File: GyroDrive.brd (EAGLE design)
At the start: 15.4 x 13.7 mm, 41 parts, among them IC1 AD8235, IC2 AD8235, IC3 AD8235, IC4 AD8235

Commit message: Removed copper from underneath MPU-9250
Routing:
- net DGND: track 19.3 -> 16.8 mm
- net VDD: track 16.7 -> 15.4 mm, vias 5 -> 6
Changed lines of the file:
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@@
 <wire x1="5.715" y1="3.81" x2="5.715" y2="4.826" width="0.1524" layer="16"/>
 <via x="5.715" y="4.826" extent="1-16" drill="0.254"/>
-<wire x1="5.715" y1="4.826" x2="5.715" y2="4.572" width="0" layer="19" extent="1-16"/>
 <wire x1="10.791" y1="3.81" x2="10.791" y2="4.826" width="0.1524" layer="16"/>
 <wire x1="10.791" y1="4.826" x2="10.795" y2="4.826" width="0.1524" layer="16"/>
 <via x="10.795" y="4.826" extent="1-16" drill="0.254"/>
-<wire x1="10.795" y1="4.826" x2="10.795" y2="4.699" width="0" layer="19" extent="1-16"/>
 <wire x1="10.791" y1="3.81" x2="10.791" y2="3.294" width="0.1524" layer="16"/>
 <wire x1="10.791" y1="3.294" x2="10.783" y2="3.294" width="0.1524" layer="16"/>
@@
 <wire x1="8.251" y1="4.826" x2="8.255" y2="4.826" width="0.1524" layer="16"/>
 <via x="8.255" y="4.826" extent="1-16" drill="0.254"/>
-<wire x1="8.255" y1="4.826" x2="8.255" y2="4.699" width="0" layer="19" extent="1-16"/>
 <wire x1="13.3056" y1="3.8608" x2="13.3056" y2="4.826" width="0.1524" layer="16"/>
 <wire x1="13.3056" y1="4.826" x2="13.335" y2="4.826" width="0.1524" layer="16"/>
 <via x="13.335" y="4.826" extent="1-16" drill="0.254"/>
-<wire x1="13.335" y1="4.826" x2="13.335" y2="4.699" width="0" layer="19" extent="1-16"/>
 <wire x1="13.3056" y1="3.8608" x2="13.3056" y2="3.294" width="0.1524" layer="16"/>
 <wire x1="13.3056" y1="3.294" x2="13.323" y2="3.294" width="0.1524" layer="16"/>
@@
 <wire x1="8.767" y1="4.445" x2="8.763" y2="4.445" width="0.1524" layer="16"/>
 <via x="8.763" y="4.445" extent="1-16" drill="0.254"/>
-<wire x1="8.763" y1="4.445" x2="8.763" y2="4.318" width="0" layer="19" extent="1-16"/>
 <wire x1="11.823" y1="2.794" x2="11.303" y2="2.794" width="0.1524" layer="16"/>
 <wire x1="11.303" y1="2.794" x2="11.303" y2="3.294" width="0.1524" layer="16"/>
@@
 <wire x1="11.303" y1="3.81" x2="11.303" y2="4.445" width="0.1524" layer="16"/>
 <via x="11.303" y="4.445" extent="1-16" drill="0.254"/>
-<wire x1="11.303" y1="4.445" x2="11.303" y2="4.318" width="0" layer="19" extent="1-16"/>
 <wire x1="11.307" y1="3.81" x2="11.307" y2="3.294" width="0.1524" layer="16"/>
 <wire x1="11.307" y1="3.294" x2="11.303" y2="3.294" width="0.1524" layer="16"/>
@@
 <wire x1="6.223" y1="3.814" x2="6.223" y2="4.445" width="0.1524" layer="16"/>
 <via x="6.223" y="4.445" extent="1-16" drill="0.254"/>
-<wire x1="6.223" y1="4.445" x2="6.223" y2="4.318" width="0" layer="19" extent="1-16"/>
 <wire x1="6.223" y1="3.302" x2="6.227" y2="3.306" width="0.1524" layer="16"/>
 <wire x1="6.227" y1="3.306" x2="6.227" y2="3.81" width="0.1524" layer="16"/>
@@
 <wire x1="3.683" y1="3.814" x2="3.683" y2="4.826" width="0.1524" layer="16"/>
 <via x="3.683" y="4.826" extent="1-16" drill="0.254"/>
-<wire x1="3.683" y1="4.826" x2="3.683" y2="4.699" width="0" layer="19" extent="1-16"/>
 <wire x1="3.683" y1="3.302" x2="3.687" y2="3.306" width="0.1524" layer="16"/>
 <wire x1="3.687" y1="3.306" x2="3.687" y2="3.81" width="0.1524" layer="16"/>
@@
 <wire x1="7.747" y1="3.81" x2="7.747" y2="4.445" width="0.1524" layer="16"/>
 <via x="7.747" y="4.445" extent="1-16" drill="0.254"/>
-<wire x1="7.747" y1="4.445" x2="7.747" y2="4.191" width="0" layer="19" extent="1-16"/>
 <wire x1="10.291" y1="3.81" x2="10.291" y2="4.445" width="0.1524" layer="16"/>
 <wire x1="10.291" y1="4.445" x2="10.287" y2="4.445" width="0.1524" layer="16"/>
 <via x="10.287" y="4.445" extent="1-16" drill="0.254"/>
-<wire x1="10.287" y1="4.445" x2="10.287" y2="4.318" width="0" layer="19" extent="1-16"/>
 <wire x1="10.291" y1="3.81" x2="10.291" y2="3.294" width="0.1524" layer="16"/>
 <wire x1="10.291" y1="3.294" x2="10.283" y2="3.294" width="0.1524" layer="16"/>
@@
 <wire x1="9.267" y1="4.826" x2="9.271" y2="4.826" width="0.1524" layer="16"/>
 <via x="9.271" y="4.826" extent="1-16" drill="0.254"/>
-<wire x1="9.271" y1="4.826" x2="9.271" y2="4.699" width="0" layer="19" extent="1-16"/>
 <wire x1="11.807" y1="3.81" x2="11.807" y2="4.826" width="0.1524" layer="16"/>
 <wire x1="11.807" y1="4.826" x2="11.811" y2="4.826" width="0.1524" layer="16"/>
 <via x="11.811" y="4.826" extent="1-16" drill="0.254"/>
-<wire x1="11.811" y1="4.826" x2="11.811" y2="4.699" width="0" layer="19" extent="1-16"/>
 <wire x1="12.8056" y1="3.8608" x2="12.8056" y2="4.445" width="0.1524" layer="16"/>
 <wire x1="12.8056" y1="4.445" x2="12.827" y2="4.445" width="0.1524" layer="16"/>
 <via x="12.827" y="4.445" extent="1-16" drill="0.254"/>
-<wire x1="12.827" y1="4.445" x2="12.827" y2="4.318" width="0" layer="19" extent="1-16"/>
 <wire x1="12.8056" y1="3.8608" x2="12.8056" y2="3.294" width="0.1524" layer="16"/>
 <wire x1="12.8056" y1="3.294" x2="12.823" y2="3.294" width="0.1524" layer="16"/>
@@
 <wire x1="6.731" y1="3.814" x2="6.731" y2="4.826" width="0.1524" layer="16"/>
 <via x="6.731" y="4.826" extent="1-16" drill="0.254"/>
-<wire x1="6.731" y1="4.826" x2="6.731" y2="4.699" width="0" layer="19" extent="1-16"/>
 <wire x1="5.211" y1="3.81" x2="5.207" y2="3.814" width="0.1524" layer="16"/>
 <wire x1="5.207" y1="3.814" x2="5.207" y2="4.445" width="0.1524" layer="16"/>
 <via x="5.207" y="4.445" extent="1-16" drill="0.254"/>
-<wire x1="5.207" y1="4.445" x2="5.207" y2="4.191" width="0" layer="19" extent="1-16"/>
 <wire x1="5.211" y1="3.81" x2="5.203" y2="3.802" width="0.1524" layer="16"/>
 <wire x1="5.203" y1="3.802" x2="5.203" y2="3.294" width="0.1524" layer="16"/>
@@
 <wire x1="4.191" y1="3.814" x2="4.191" y2="4.445" width="0.1524" layer="16"/>
 <via x="4.191" y="4.445" extent="1-16" drill="0.254"/>
-<wire x1="4.191" y1="4.445" x2="4.191" y2="4.318" width="0" layer="19" extent="1-16"/>
 </signal>
 <signal name="S1">
@@
 <wire x1="11.034" y1="11.6078" x2="10.684" y2="11.557" width="0.1524" layer="1"/>
 <wire x1="10.684" y1="11.557" x2="10.684" y2="10.6932" width="0.1524" layer="1"/>
-<wire x1="10.684" y1="9.6932" x2="10.684" y2="10.6932" width="0.1524" layer="1"/>
 <contactref element="U$3" pad="2"/>
 <contactref element="C13" pad="2"/>
@@
 <wire x1="10.834" y1="12.7" x2="9.906" y2="12.7" width="0.254" layer="1"/>
 <via x="9.906" y="12.7" extent="1-16" drill="0.254"/>
-<wire x1="10.084" y1="9.6932" x2="10.684" y2="9.6932" width="0.1524" layer="1"/>
-<wire x1="10.684" y1="9.6932" x2="10.6934" y2="9.6932" width="0.1524" layer="1"/>
-<wire x1="10.6934" y1="9.6932" x2="10.668" y2="11.557" width="0.1524" layer="1"/>
 <wire x1="10.668" y1="11.557" x2="10.834" y2="11.557" width="0.1524" layer="1"/>
 <wire x1="10.834" y1="11.557" x2="10.834" y2="12.7" width="0.254" layer="1"/>
@@
 <via x="5.207" y="6.731" extent="1-16" drill="0.254"/>
 <wire x1="5.207" y1="6.731" x2="5.207" y2="7.366" width="0.254" layer="15"/>
+<wire x1="10.084" y1="9.6932" x2="9.144" y2="9.6932" width="0.1524" layer="1"/>
+<wire x1="9.144" y1="9.6932" x2="9.144" y2="9.652" width="0.1524" layer="1"/>
 </signal>
 <signal name="SDA">
@@
 <wire x1="13.284" y1="8.8932" x2="14.4526" y2="8.8932" width="0.1524" layer="1"/>
 <wire x1="14.4526" y1="8.8932" x2="14.4526" y2="8.494" width="0.1524" layer="1"/>
-<wire x1="10.084" y1="8.8932" x2="10.684" y2="8.8932" width="0.1524" layer="1"/>
-<wire x1="10.684" y1="8.8932" x2="10.684" y2="7.4932" width="0.1524" layer="1"/>
 <contactref element="U$3" pad="5"/>
 <contactref element="C14" pad="1"/>
@@
 <wire x1="10.084" y1="8.8932" x2="10.084" y2="8.89" width="0.1524" layer="1"/>
 <wire x1="10.084" y1="8.89" x2="9.525" y2="8.89" width="0.1524" layer="1"/>
-<wire x1="9.525" y1="8.89" x2="9.525" y2="9.017" width="0.1524" layer="1"/>
-<wire x1="9.525" y1="9.017" x2="9.398" y2="9.017" width="0.1524" layer="1"/>
+<wire x1="9.525" y1="8.89" x2="9.398" y2="9.017" width="0.1524" layer="1"/>
 <via x="9.398" y="9.017" extent="1-16" drill="0.254"/>
 <wire x1="14.478" y1="8.651" x2="14.732" y2="8.636" width="0.1524" layer="1"/>
+<wire x1="10.684" y1="7.4932" x2="10.668" y2="7.4932" width="0.1524" layer="1"/>
+<wire x1="10.668" y1="7.4932" x2="10.668" y2="6.8326" width="0.1524" layer="1"/>
+<via x="10.668" y="6.8326" extent="1-16" drill="0.254"/>
+<wire x1="10.668" y1="6.8326" x2="10.541" y2="6.858" width="0.1524" layer="2"/>
 </signal>
 <signal name="SDAOUT">

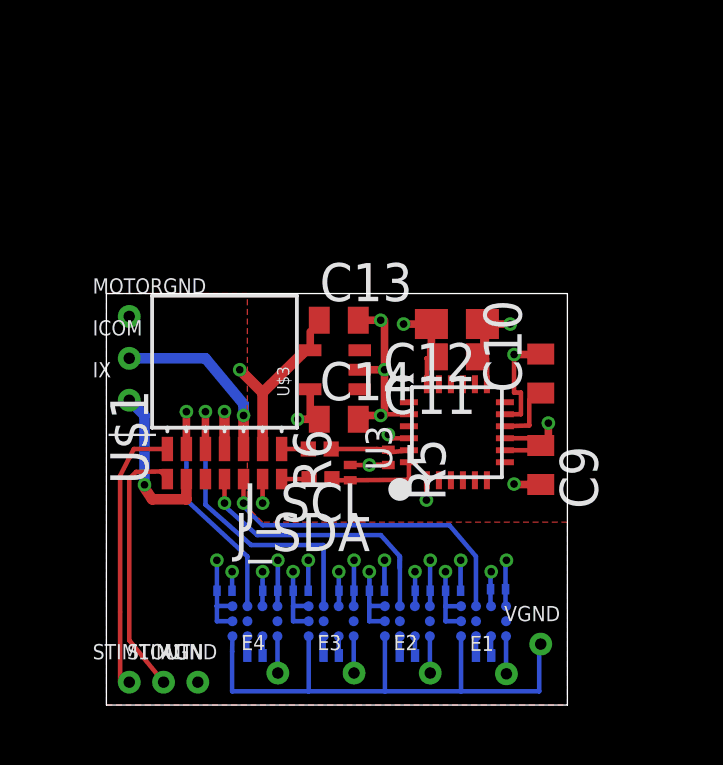
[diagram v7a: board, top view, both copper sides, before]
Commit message: Added jumper between VGND and AGND
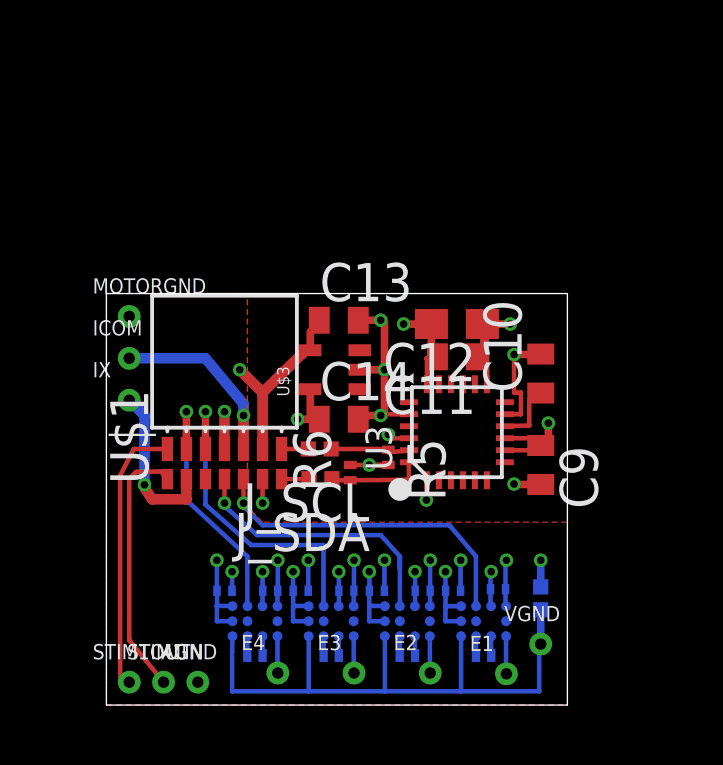
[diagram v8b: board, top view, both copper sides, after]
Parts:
- added J_VGND: (no value), michael-stetner:SJ
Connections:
- net AGND: now also J_VGND.2
- net VGND: now also J_VGND.1
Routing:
- net VGND: track 19.2 -> 20.3 mm
- net AGND: track 11.6 -> 12.7 mm, vias 9 -> 10
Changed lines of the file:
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@@
 <element name="E4" library="michael-stetner" package="30MIL/15MIL" value="" x="5.715" y="1.0668"/>
 <element name="VGND" library="michael-stetner" package="30MIL/15MIL" value="" x="14.478" y="2.032"/>
+<element name="J_VGND" library="michael-stetner" package="SJ" value="" x="14.478" y="3.556" rot="MR90"/>
 </elements>
 <signals>
@@
 <wire x1="4.191" y1="3.814" x2="4.191" y2="4.445" width="0.1524" layer="16"/>
 <via x="4.191" y="4.445" extent="1-16" drill="0.254"/>
+<contactref element="J_VGND" pad="2"/>
+<wire x1="14.478" y1="3.937" x2="14.478" y2="4.826" width="0.254" layer="16"/>
+<via x="14.478" y="4.826" extent="1-16" drill="0.254"/>
+<wire x1="14.478" y1="4.826" x2="14.478" y2="4.953" width="0.254" layer="15"/>
 </signal>
 <signal name="S1">
@@
 <wire x1="11.823" y1="2.294" x2="11.823" y2="0.4572" width="0.1524" layer="16"/>
 <wire x1="6.743" y1="2.294" x2="6.743" y2="0.4572" width="0.1524" layer="16"/>
+<contactref element="J_VGND" pad="1"/>
+<wire x1="14.478" y1="3.175" x2="14.478" y2="2.032" width="0.254" layer="16"/>
 </signal>
 <signal name="S3">
